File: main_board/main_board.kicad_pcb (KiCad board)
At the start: 2 copper layers, 132 parts, among them J1 stepper 0, J10 24VDC output 5, J11 5VDC output 0, J12 5VDC output 1, J13 5VDC output 2, J14 5VDC output 3, J15 5VDC output 4, J16 5VDC output 5, J17 temperature measure 0, J18 temperature measure 1, J19 I2C, J2 stepper 1, J20 I2C, J21 I2C, J22 I2C, J23 hall measure 0, J24 weight measure 0, J25 light measure 0, J26 24VDC_in, J27 24VDC to 5VDC step down, J28 24VDC, J29 24VDC, J3 stepper 2, J30 24VDC, J31 5VDC, J32 5VDC, J33 5VDC, J34 hall measure 1, J35 reflective sensor 0, J36 24VDC, J37 24VDC, J38 24VDC, J39 5VDC, J4 stepper 3, J40 5VDC, J41 5VDC, J5 24VDC output 0, J6 24VDC output 1, J7 24VDC output 2, J8 24VDC output 3, J9 24VDC output 4, Q1 Q_NMOS_GDS, Q10 BS170, Q11 BS170, Q12 BS170, Q2 Q_NMOS_GDS, Q3 Q_NMOS_GDS, Q4 Q_NMOS_GDS, Q5 Q_NMOS_GDS, Q6 Q_NMOS_GDS, Q7 BS170, Q8 BS170, Q9 BS170, SW1 Rotary_Encoder_Switch, U1 ESP32-DEVKITC-32D, U2 PCA9685PW

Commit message: PCB v1
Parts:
- moved R25 211.5 mm to (66.0, 102.6), turned to 270 degrees
- moved R26 200.4 mm to (76.2, 102.6), turned to 270 degrees
- moved C16 199.5 mm to (67.3, 81.3), turned to 270 degrees
- moved J5 199.0 mm to (172.7, 52.1), turned to 270 degrees
- moved C6 197.2 mm to (71.1, 107.9), turned to 90 degrees
- moved R27 196.9 mm to (64.8, 111.5), turned to 270 degrees
- moved R31 191.7 mm to (70.1, 111.8), turned to 180 degrees
- moved R38 190.5 mm to (72.7, 86.4), turned to 180 degrees
- moved R40 190.2 mm to (72.7, 91.4)
- moved R36 189.7 mm to (82.8, 90.2), turned to 180 degrees
- moved R1 187.2 mm to (150.1, 57.1), turned to 180 degrees
- moved R28 187.0 mm to (74.9, 111.5), turned to 270 degrees
- moved C7 186.8 mm to (81.3, 107.9), turned to 90 degrees
- moved R32 181.4 mm to (80.3, 111.8), turned to 180 degrees
- moved R2 180.5 mm to (144.8, 55.6), turned to 270 degrees
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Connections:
- R15 pad 2: 5VDC_output0 -> 5VDC_output1
- R16 pad 2: 5VDC_output0 -> 5VDC_output1
- R17 pad 2: 5VDC_output0 -> 5VDC_output2
- R18 pad 2: 5VDC_output0 -> 5VDC_output2
- R19 pad 2: 5VDC_output0 -> 5VDC_output3
- R20 pad 2: 5VDC_output0 -> 5VDC_output3
- R21 pad 2: 5VDC_output0 -> 5VDC_output4
- R22 pad 2: 5VDC_output0 -> 5VDC_output4
- R23 pad 2: 5VDC_output0 -> 5VDC_output5
- R24 pad 2: 5VDC_output0 -> 5VDC_output5
- U2 pad 17: stepperON -> 5VDC_output4
- U2 pad 18: stepperErr -> 5VDC_output5
- U2 pad 19: LEDcon0 -> stepperON
- U2 pad 20: Net-(U2-Pad20) -> stepperErr
- U2 pad 21: Net-(U2-Pad21) -> LEDcon0
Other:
- board outline added: 146 x 111.8 mm

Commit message: PCB changes
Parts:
- removed C10, C11: 100uF, Capacitor_THT:CP_Radial_D6.3mm_P2.50mm
- removed R34, R35: 10k, Resistor_SMD:R_1206_3216Metric_Pad1.30x1.75mm_HandSolder
- removed SW1: Rotary_Encoder_Switch, Rotary_Encoder:RotaryEncoder_Alps_EC11E-Switch_Vertical_H20mm
- added J42: Conn_01x05_Male, Connector_PinHeader_2.54mm:PinHeader_1x05_P2.54mm_Vertical, F.Cu at (143.5, 64.8)
- R39: moved to F.Cu
- moved R36 80.5 mm to (132.4, 26.7)
- moved C16 80.5 mm to (116.8, 17.8)
- moved J35 80.5 mm to (127.0, 19.1)
- moved R38 80.5 mm to (122.2, 22.9)
- moved R40 80.5 mm to (122.2, 27.9)
- moved D1 64.7 mm to (165.1, 116.8), turned to 270 degrees
- moved Q1 62.3 mm to (160.0, 119.4)
- moved R1 62.3 mm to (153.9, 119.4)
- moved J5 62.2 mm to (172.7, 114.3)
- moved R2 60.5 mm to (152.4, 115.6)
- moved J25 58.6 mm to (108.0, 27.9)
- moved J36 54.6 mm to (174.0, 35.6)
- moved J37 54.6 mm to (170.2, 35.6)
- moved J38 54.6 mm to (166.4, 35.6)
- moved Q6 52.2 mm to (160.0, 62.2)
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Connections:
- C12 pad 2: encb -> enca
- C13 pad 1: enca -> encb
- C8 pad 1: +3V3 -> button
- C8 pad 2: button -> +3V3
- J24 pad 3: Net-(J24-Pad3) -> DT
- J25 pad 2: Net-(J25-Pad2) -> AO

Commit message: routs added
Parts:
- moved J12 87.5 mm to (172.7, 39.4), turned to 270 degrees
- moved D8 76.1 mm to (165.1, 41.9), turned to 270 degrees
- moved J11 72.9 mm to (172.7, 50.8), turned to 270 degrees
- moved Q8 68.2 mm to (160.0, 44.5), turned to 90 degrees
- moved R15 63.0 mm to (153.9, 39.4), turned to 180 degrees
- moved D7 61.6 mm to (165.1, 53.3), turned to 270 degrees
- moved R16 57.9 mm to (152.4, 44.7), turned to 90 degrees
- moved Q7 53.5 mm to (160.0, 55.9), turned to 90 degrees
- moved R13 49.4 mm to (153.9, 50.8), turned to 180 degrees
- moved R14 43.6 mm to (152.4, 56.2), turned to 90 degrees
- moved R1 42.6 mm to (128.3, 85.4), turned to 90 degrees
- moved Q1 42.3 mm to (128.3, 91.4), turned to 0 degrees
- moved J5 40.7 mm to (133.3, 104.1), turned to 180 degrees
- moved D1 39.8 mm to (130.8, 96.5), turned to 180 degrees
- moved R2 37.5 mm to (132.4, 83.8), turned to 180 degrees
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
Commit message: routs added
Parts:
- added H1: MountingHole, MountingHole:MountingHole_3.2mm_M3, F.Cu at (175.0, 18.0)
- added H2: MountingHole, MountingHole:MountingHole_3.2mm_M3, F.Cu at (40.0, 18.0)
- added H3: MountingHole, MountingHole:MountingHole_3.2mm_M3, F.Cu at (40.0, 108.0)
- added H4: MountingHole, MountingHole:MountingHole_3.2mm_M3, F.Cu at (175.0, 108.0)
- moved D13 5.08 mm to (128.3, 20.4)
- moved C16 3.81 mm to (113.0, 17.8)
- moved F1 3.81 mm to (157.5, 21.6)
- moved J35 3.81 mm to (123.2, 19.1)
- moved R36 3.81 mm to (128.6, 26.7)
- moved R38 3.81 mm to (118.4, 22.9)
- moved R40 3.81 mm to (118.4, 27.9)
- moved J1 3.79 mm to (40.6, 33.0)
- moved J26 3.50 mm to (162.9, 22.9)
- moved J25 2.54 mm to (105.4, 27.9)
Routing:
- net GND: track 0.00 -> 658.6 mm
- net +24V: track 0.00 -> 389.9 mm
- net +5V: track 0.00 -> 299.4 mm
- net +3V3: track 0.00 -> 157.6 mm, vias 0 -> 3
- net stepperErr: track 0.00 -> 152.6 mm
- net stepperON: track 0.00 -> 139.8 mm
- net SDA: track 0.00 -> 81.1 mm, vias 0 -> 1
- net SCL: track 0.00 -> 79.7 mm, vias 0 -> 1
- net enca: track 0.00 -> 79.2 mm
- net Net-(R26-Pad1): track 0.00 -> 69.1 mm, vias 0 -> 1
- net STEP3: track 0.00 -> 68.0 mm
- net Net-(R25-Pad1): track 0.00 -> 65.7 mm, vias 0 -> 1
- net DIR3: track 0.00 -> 61.3 mm
- net button: track 0.00 -> 54.5 mm, vias 0 -> 1
- net OE: track 0.00 -> 54.3 mm, vias 0 -> 1
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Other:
- board size 146 x 111.8 mm -> 145 x 100 mm

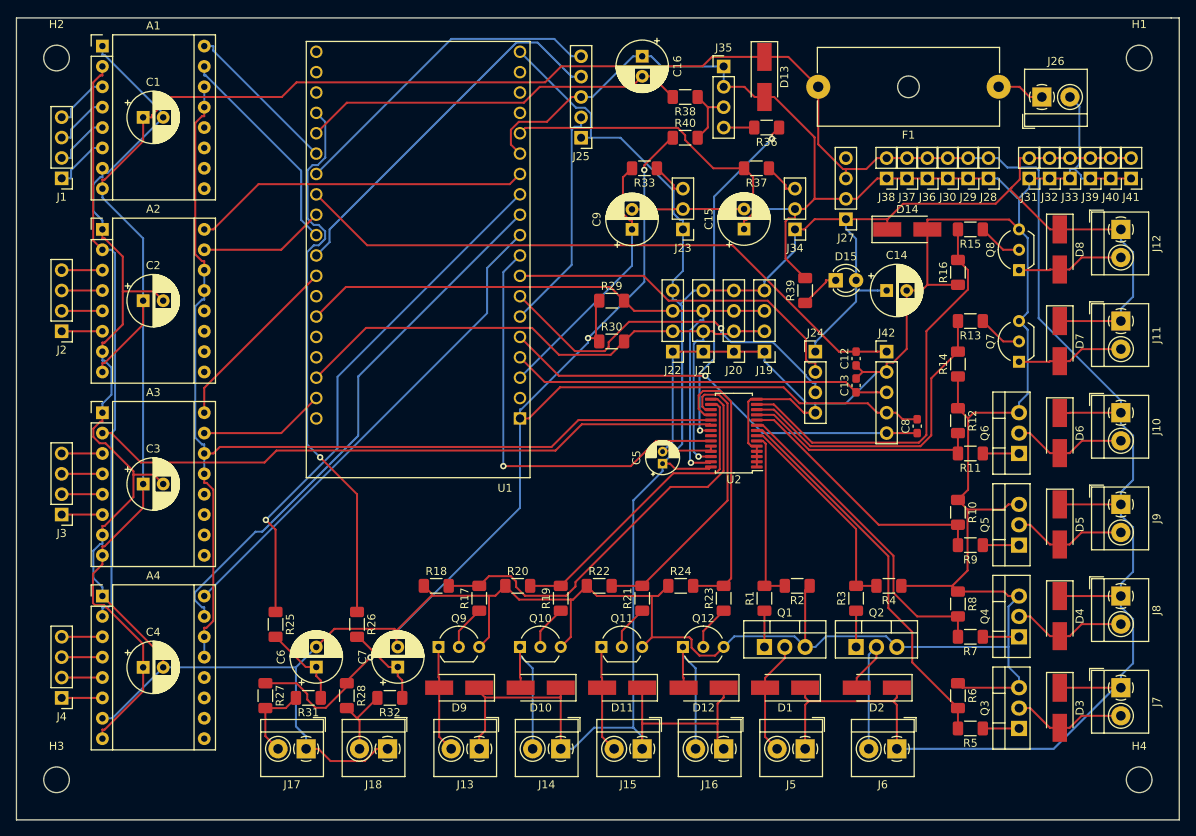
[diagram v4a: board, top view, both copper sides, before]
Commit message: making pcb smaller
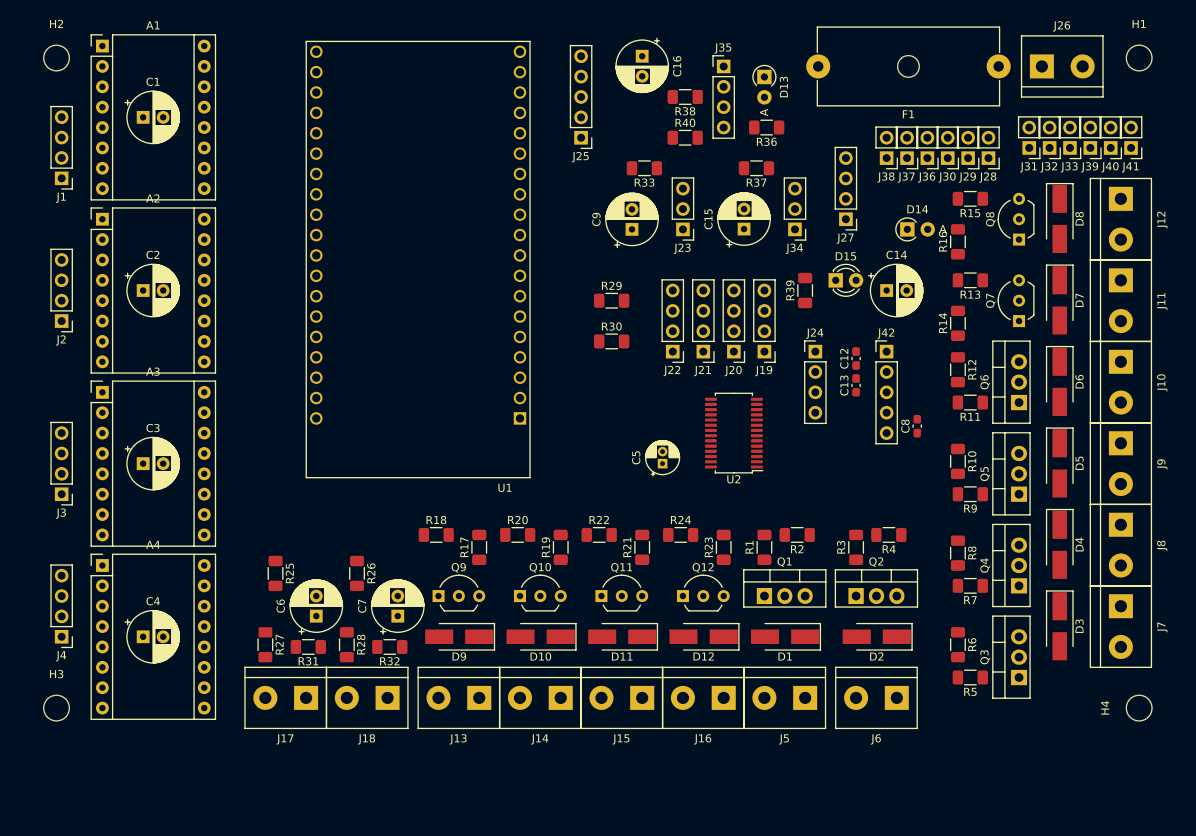
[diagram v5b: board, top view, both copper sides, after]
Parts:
- D13, D14: footprint Diode_SMD:D_SMA_Handsoldering -> Diode_THT:D_A-405_P2.54mm_Vertical_AnodeUp
- J10, J11, J12, J13, J14, J15, J16, J17, J18, J26, J5, J6, J7, J8, J9: footprint TerminalBlock_4Ucon:TerminalBlock_4Ucon_1x02_P3.50mm_Horizontal -> TerminalBlock:TerminalBlock_bornier-2_P5.08mm
- moved D3 10.2 mm to (165.1, 88.9)
- moved J7 10.2 mm to (172.7, 86.4)
- moved H3 8.94 mm to (40.0, 99.1)
- moved H4 8.94 mm to (175.0, 99.1), turned to 90 degrees
- moved D4 8.89 mm to (165.1, 78.7)
- moved J8 8.89 mm to (172.7, 76.2)
- moved J4 7.62 mm to (40.6, 90.2)
- moved D5 7.62 mm to (165.1, 68.5)
- moved J9 7.62 mm to (172.7, 66.0)
- moved D6 6.39 mm to (165.1, 58.4)
- moved Q4 6.35 mm to (160.0, 83.8)
- moved R1 6.35 mm to (128.3, 79.0)
- moved R10 6.35 mm to (152.4, 68.3)
- moved R17 6.35 mm to (92.7, 79.0)
- moved R19 6.35 mm to (102.9, 79.0)
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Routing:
- net GND: track 658.6 -> 0.00 mm
- net +24V: track 389.9 -> 0.00 mm
- net +5V: track 299.4 -> 0.00 mm
- net +3V3: track 157.6 -> 0.00 mm, vias 3 -> 0
- net stepperErr: track 152.6 -> 0.00 mm
- net stepperON: track 139.8 -> 0.00 mm
- net SDA: track 81.1 -> 0.00 mm, vias 1 -> 0
- net SCL: track 79.7 -> 0.00 mm, vias 1 -> 0
- net enca: track 79.2 -> 0.00 mm
- net Net-(R26-Pad1): track 69.1 -> 0.00 mm, vias 1 -> 0
- net STEP3: track 68.0 -> 0.00 mm
- net Net-(R25-Pad1): track 65.7 -> 0.00 mm, vias 1 -> 0
- net DIR3: track 61.3 -> 0.00 mm
- net button: track 54.5 -> 0.00 mm, vias 1 -> 0
- net OE: track 54.3 -> 0.00 mm, vias 1 -> 0
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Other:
- board outline removed

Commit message: PCB update
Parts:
- moved J6 1.27 mm to (143.5, 97.8)
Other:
- board outline added: 145 x 91 mm
- net class 24VDC added: clearance 0.2, trace_width 1.5, via_dia 0.8, via_drill 0.4

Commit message: added routs
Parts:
- D1, D10, D11, D12, D2, D3, D4, D5, D6, D7, D8, D9: footprint Diode_SMD:D_SMA_Handsoldering -> Diode_THT:D_DO-15_P2.54mm_Vertical_AnodeUp
- D13, D14: footprint Diode_THT:D_A-405_P2.54mm_Vertical_AnodeUp -> Diode_THT:D_DO-15_P2.54mm_Vertical_AnodeUp
- moved J11 90.6 mm to (95.2, 92.7), turned to 180 degrees
- moved J12 88.3 mm to (105.4, 92.7), turned to 180 degrees
- moved D7 81.2 mm to (92.8, 85.1), turned to 180 degrees
- moved D8 78.0 mm to (102.9, 85.1), turned to 180 degrees
- moved Q7 75.7 mm to (90.2, 80.0), turned to 0 degrees
- moved Q8 71.5 mm to (100.3, 80.0), turned to 0 degrees
- moved R14 66.0 mm to (89.9, 72.4), turned to 0 degrees
- moved R13 65.1 mm to (95.2, 73.9), turned to 90 degrees
- moved R15 61.9 mm to (105.4, 73.9), turned to 90 degrees
- moved R16 61.1 mm to (100.0, 72.4), turned to 0 degrees
- moved J5 44.9 mm to (174.0, 78.7), turned to 270 degrees
- moved J6 42.2 mm to (174.0, 68.6), turned to 270 degrees
- moved D1 38.5 mm to (167.6, 78.7)
- moved R5 37.3 mm to (159.7, 58.4)
- moved R7 36.0 mm to (159.7, 48.3)
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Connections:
- U2 pad 10: 24VDC_output4 -> 24VDC_output2
- U2 pad 11: 24VDC_output5 -> 24VDC_output3
- U2 pad 12: 5VDC_output0 -> 24VDC_output4
- U2 pad 13: 5VDC_output1 -> 24VDC_output5
- U2 pad 15: 5VDC_output2 -> 5VDC_output0
- U2 pad 16: 5VDC_output3 -> 5VDC_output1
- U2 pad 17: 5VDC_output4 -> 5VDC_output2
- U2 pad 18: 5VDC_output5 -> 5VDC_output3
- U2 pad 6: 24VDC_output0 -> 5VDC_output4
- U2 pad 7: 24VDC_output1 -> 5VDC_output5
- U2 pad 8: 24VDC_output2 -> 24VDC_output0
- U2 pad 9: 24VDC_output3 -> 24VDC_output1
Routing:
- net GND: track 0.00 -> 676.5 mm
- net +24V: track 0.00 -> 381.4 mm
- net +5V: track 0.00 -> 307.5 mm
- net +3V3: track 0.00 -> 159.5 mm, vias 0 -> 1
- net stepperErr: track 0.00 -> 143.7 mm
- net stepperON: track 0.00 -> 130.7 mm
- net enca: track 0.00 -> 90.3 mm
- net SCL: track 0.00 -> 90.0 mm, vias 0 -> 1
- net SDA: track 0.00 -> 89.3 mm, vias 0 -> 1
- net Net-(R26-Pad1): track 0.00 -> 87.3 mm
- net button: track 0.00 -> 64.3 mm
- net STEP3: track 0.00 -> 62.8 mm
- net 24VDC_output5: track 0.00 -> 60.0 mm
- net encb: track 0.00 -> 57.0 mm
- net DIR3: track 0.00 -> 56.6 mm
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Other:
- board size 145 x 91 mm -> 146 x 87 mm

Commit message: routs added
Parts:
- J10: value 24VDC output 5 -> 24VDCout5
- J11: value 5VDC output 0 -> 5VDCout0
- J12: value 5VDC output 1 -> 5VDCout1
- J13: value 5VDC output 2 -> 5VDCout2
- J14: value 5VDC output 3 -> 5VDCout3
- J15: value 5VDC output 4 -> 5VDCout4
- J16: value 5VDC output 5 -> 5VDCout5
- J5: value 24VDC output 0 -> 24VDCout0
- J6: value 24VDC output 1 -> 24VDCout1
- J7: value 24VDC output 2 -> 24VDCout2
- J8: value 24VDC output 3 -> 24VDCout3
- J9: value 24VDC output 4 -> 24VDCout4
- moved C8 10.2 mm to (137.2, 63.5)
- moved Q1 6.48 mm to (160.0, 78.7)
- moved Q2 6.48 mm to (160.0, 68.6)
- moved Q4 6.48 mm to (160.0, 48.3)
- moved Q5 6.48 mm to (160.0, 38.1)
- moved Q6 6.48 mm to (160.0, 27.9)
- moved Q3 6.48 mm to (160.0, 58.4)
- moved R10 5.78 mm to (154.9, 37.8), turned to 270 degrees
- moved R4 5.78 mm to (154.9, 68.3), turned to 270 degrees
- moved R6 5.78 mm to (154.9, 58.1), turned to 270 degrees
- moved R8 5.78 mm to (154.9, 48.0), turned to 270 degrees
- moved R12 5.78 mm to (154.9, 27.7), turned to 270 degrees
- moved R7 5.68 mm to (157.2, 53.3)
- moved R11 5.68 mm to (157.2, 33.0)
- moved R1 5.68 mm to (157.2, 83.8)
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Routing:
- net +24V: track 381.4 -> 426.3 mm
- net SDA: track 89.3 -> 118.8 mm, vias 1 -> 2
- net GND: track 676.5 -> 703.5 mm
- net SCL: track 90.0 -> 111.8 mm, vias 1 -> 2
- net 5VDC_output3: track 29.2 -> 45.6 mm
- net +5V: track 307.5 -> 320.7 mm, vias 0 -> 1
- net +3V3: track 159.5 -> 148.0 mm, vias 1 -> 2
- net hallmeasure0: track 38.3 -> 27.1 mm
- net button: track 64.3 -> 53.5 mm, vias 0 -> 2
- net DIR3: track 56.6 -> 66.1 mm
- net 5VDC_output0: track 24.8 -> 34.1 mm
- net enca: track 90.3 -> 81.3 mm, vias 0 -> 2
- net Net-(R26-Pad1): track 87.3 -> 95.9 mm
- net LEDcon0: track 45.9 -> 38.4 mm, vias 0 -> 2
- net 24VDC_output2: track 50.8 -> 43.4 mm
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- added copper zone on B.Cu, net GND
- added copper zone on F.Cu, net GND
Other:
- board size 146 x 87 mm -> 145 x 87 mm
- board text added: "+"
